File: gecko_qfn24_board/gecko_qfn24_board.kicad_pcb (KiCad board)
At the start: 2 copper layers, 15.2 x 22.9 mm, 9 parts, among them P1 CONN_01X09, P2 CONN_01X09, P3 USB_B, U1 EFM32HG309

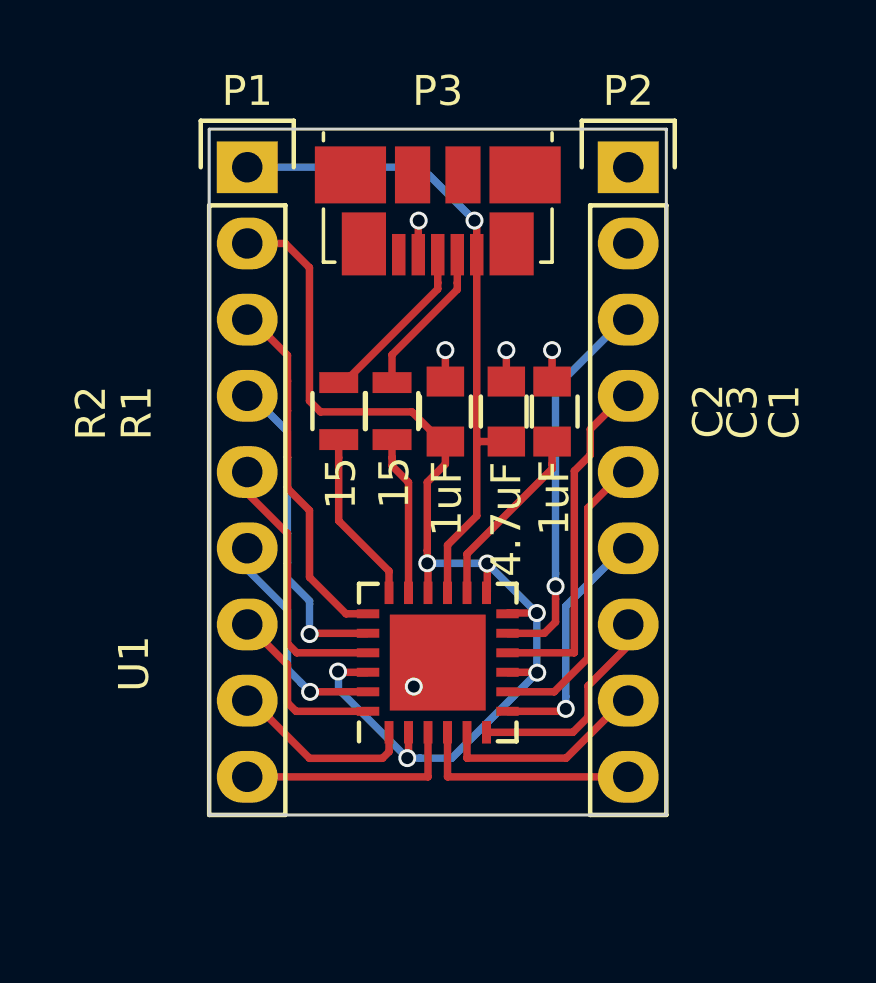
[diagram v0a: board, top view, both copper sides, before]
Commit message: fixed printf
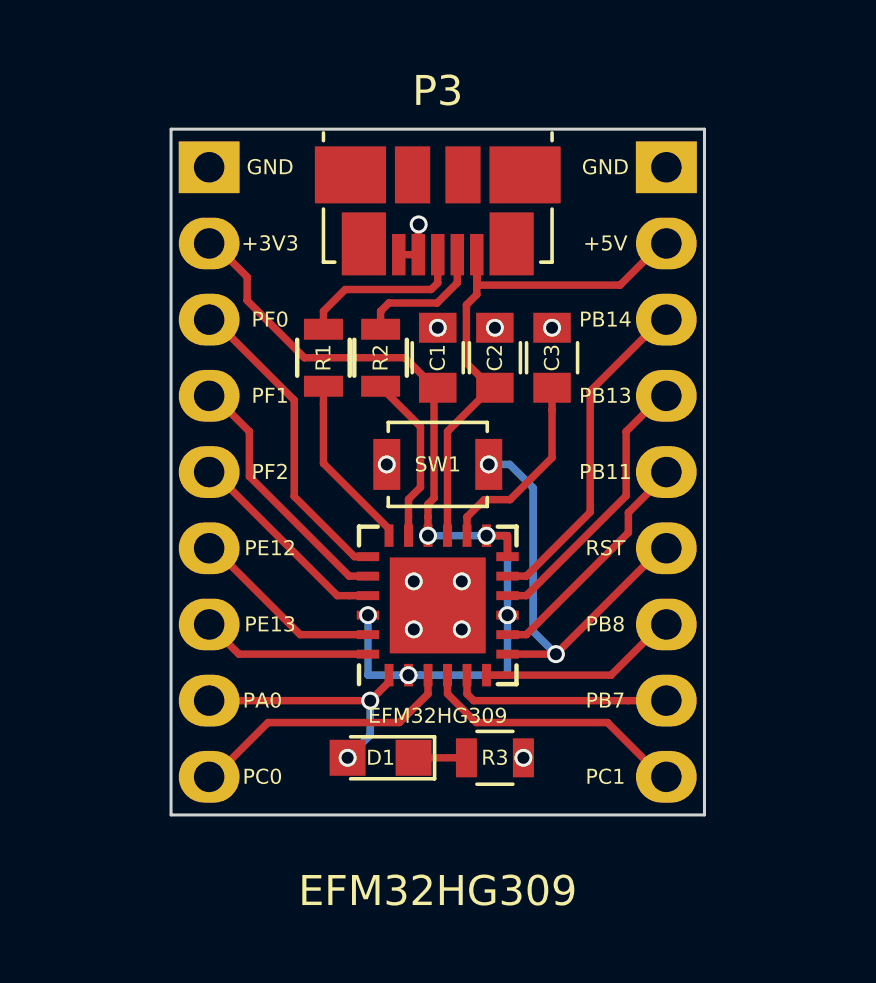
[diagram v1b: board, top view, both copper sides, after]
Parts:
- added D1: LED, LEDs:LED_0805, F.Cu at (145.4, 117.5)
- added R3: R_Small, Resistors_SMD:R_0805, F.Cu at (149.2, 117.5)
- added SW1: RST, Buttons_Switches_SMD:SW_SPST_B3U-1000P, F.Cu at (147.3, 107.7)
- C2: value 1uF -> 4.7uF
- C3: value 4.7uF -> 1uF
- P1, P2: moved to B.Cu
- moved C1 4.21 mm to (147.3, 104.1)
- moved R1 2.90 mm to (143.5, 104.1)
- moved C2 2.44 mm to (149.2, 104.1)
- moved C3 2.35 mm to (151.1, 104.1)
- moved R2 2.26 mm to (145.4, 104.1)
- moved EFM32HG309 1.91 mm to (147.3, 112.4)
- moved P1 1.27 mm to (139.7, 97.8), turned to 180 degrees
- moved P2 1.27 mm to (154.9, 97.8), turned to 180 degrees
- renumbered U1 to EFM32HG309
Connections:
- net Net-(P1-Pad3) renamed /PF0
- net Net-(P1-Pad4) renamed /PF1
- net Net-(P1-Pad5) renamed /PF2
- net Net-(P1-Pad6) renamed /PE12
- net Net-(P1-Pad7) renamed /PE13
- net Net-(P1-Pad8) renamed /PA0
- net Net-(P1-Pad9) renamed /PC0
- net Net-(P2-Pad3) renamed /PB14
- net Net-(P2-Pad4) renamed /PB13
- net Net-(P2-Pad5) renamed /PB11
- net Net-(P2-Pad6) renamed /RST
- net Net-(P2-Pad7) renamed /PB8
- net Net-(P2-Pad8) renamed /PB7
- net Net-(P2-Pad9) renamed /PC1
- C1 pad 1: Net-(C1-Pad1) -> +3V3
- C2 pad 1: +3V3 -> +5V
- C3 pad 1: +5V -> Net-(C3-Pad1)
- EFM32HG309 pad 14: Net-(C1-Pad1) -> Net-(C3-Pad1)
- EFM32HG309 pad 17: Net-(R1-Pad2) -> Net-(R2-Pad2)
- EFM32HG309 pad 18: Net-(R2-Pad2) -> Net-(R1-Pad2)
- P1 pad 1: +5V -> GND
- P2 pad 2: GND -> +5V
- P3 pad 5: Net-(P3-Pad5) -> GND
- R1 pad 1: Net-(P3-Pad2) -> Net-(P3-Pad3)
- R2 pad 1: Net-(P3-Pad3) -> Net-(P3-Pad2)
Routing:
- net +3V3: track 38.1 -> 30.5 mm, vias 6 -> 5
- net Net-(C3-Pad1): track 0.00 -> 6.61 mm
- net Net-(C1-Pad1): track 6.22 -> 0.00 mm
- net /RST: track 9.14 -> 14.4 mm, vias 1 -> 2
- net +5V: track 22.4 -> 18.4 mm, vias 1 -> 0
- net GND: track 4.29 -> 1.67 mm, vias 5 -> 10
- net /PB13: track 11.9 -> 9.31 mm
- net /PA0: track 6.27 -> 8.70 mm, vias 0 -> 2
- net /PF2: track 9.39 -> 7.00 mm
- net /PF1: track 11.0 -> 8.66 mm, vias 1 -> 0
- net /PB11: track 10.3 -> 7.98 mm
- net /PF0: track 12.6 -> 10.4 mm
- net Net-(D1-Pad1): track 0.00 -> 1.76 mm
- net /PB14: track 13.0 -> 11.2 mm, vias 1 -> 0
- net /PE12: track 8.23 -> 6.49 mm, vias 1 -> 0
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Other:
- board size 15.2 x 22.9 mm -> 17.8 x 22.9 mm
- board text added: "+3V3"
- board text added: "EFM32HG309"
- board text added: "EFM32HG309 BOARD v0.3 By: Jonas 'Kokjo' Rudloff Email: jonas.t.rudloff@gmail.com"
- board text added: "RST"
- board text removed: "15"
- board text removed: "1uF"
- board text removed: "3V3"
- board text removed: "4.7uF"
- board text removed: "RESET"
